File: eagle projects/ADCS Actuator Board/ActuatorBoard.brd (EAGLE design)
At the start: 91 x 91 mm, 259 parts, among them J4 OSTVN08A150, J5 OSTVN08A150, J6 OSTVN08A150, U10 TVS991, U11 BD6210F-E2, U12 ADS7841E_2K5, U13 ADS7841E_2K5, U15 TLV9051IDCKR, U16 BD6210F-E2, U17 DRV10970_MOTOR_DRIVERDRV10970, U18 DRV10970_MOTOR_DRIVERDRV10970, U19 TLV9051IDCKR, U20 DRV10970_MOTOR_DRIVERDRV10970, U21 TLV9051IDCKR, U22 BD6210F-E2, U23 TLV9051IDCKR, U24 TLV9051IDCKR, U25 ADS7841E_2K5, U26 TLV9051IDCKR, U27 ADS7841E_2K5, U28 TLV9051IDCKR, U29 TLV9051IDCKR, U30 TLV9051IDCKR, U31 TLV9051IDCKR, U32 TLV9051IDCKR, U4 ADS7841E_2K5, U6 TLV9051IDCKR, U7 TVS991, U8 TVS991, U9 ADS7841E_2K5

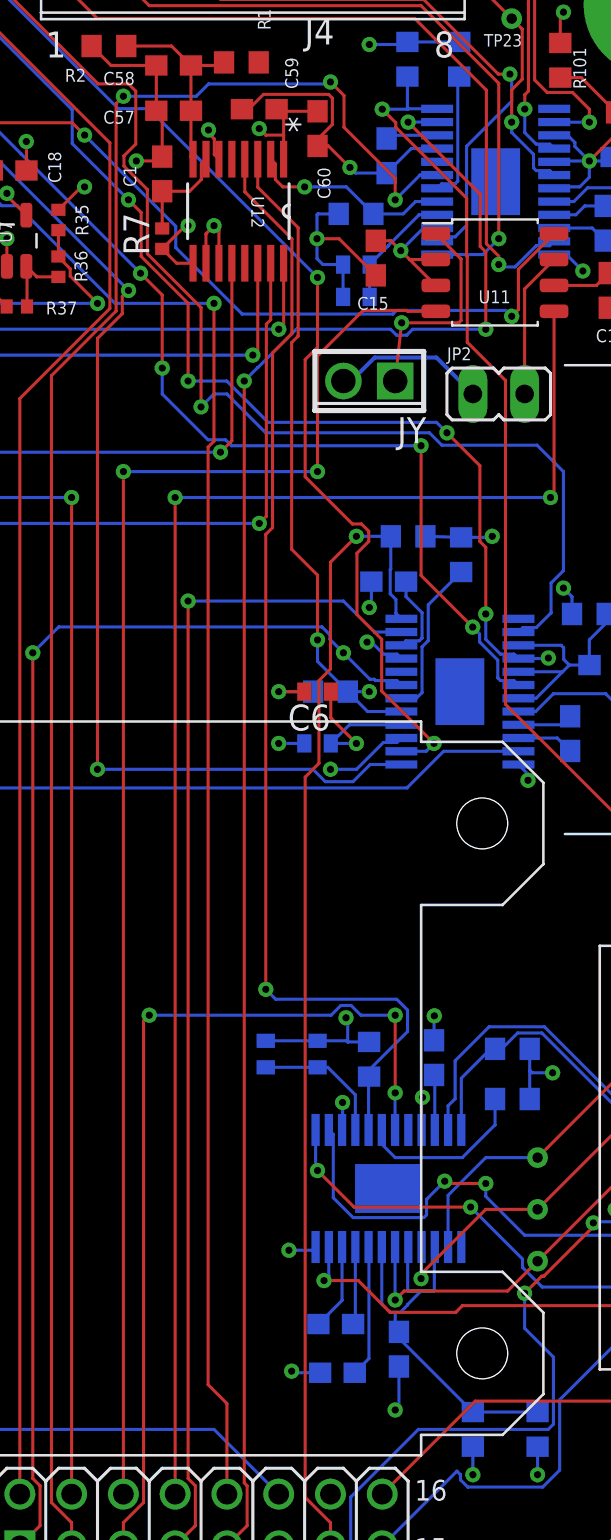
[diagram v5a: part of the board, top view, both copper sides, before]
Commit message: Fixed motordriver schematic for readability
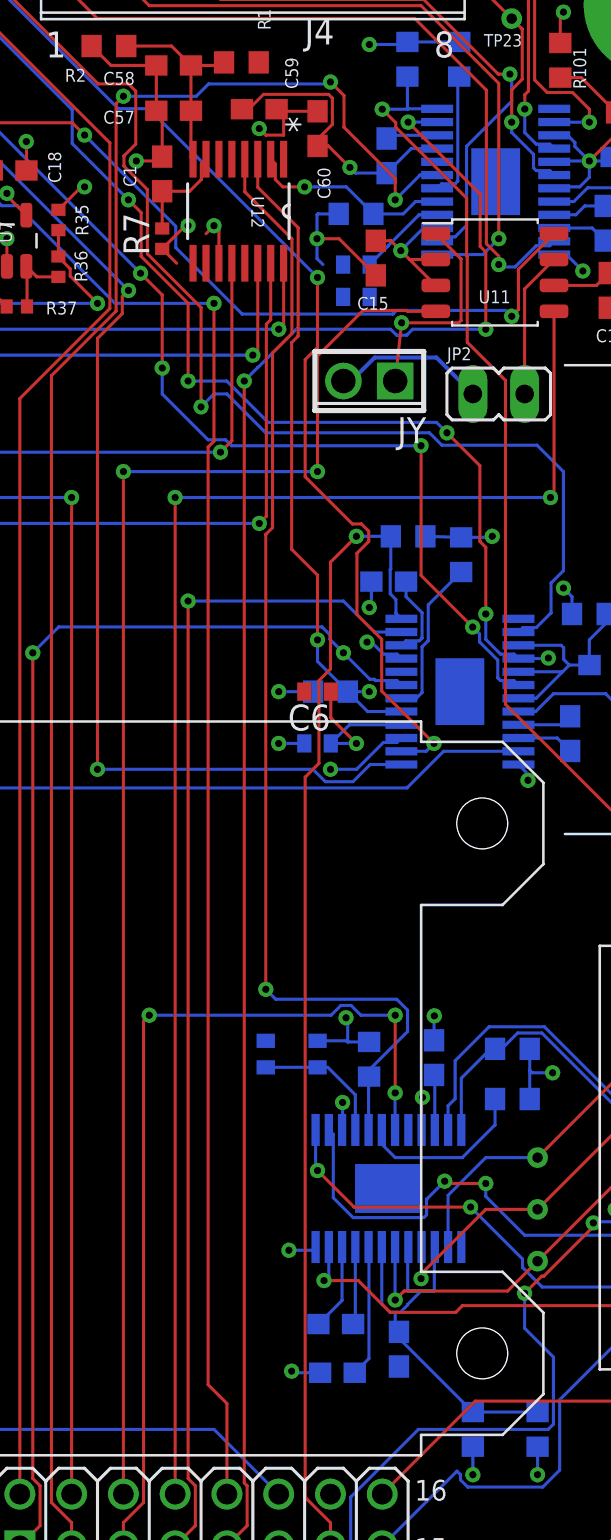
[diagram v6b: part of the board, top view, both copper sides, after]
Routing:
- net GND: track 213.5 -> 201.8 mm, vias 134 -> 132
- net +3V3: track 186.4 -> 184.4 mm
- net N$26: track 5.92 -> 4.33 mm
- net VINT/2_Z: track 20.6 -> 20.0 mm

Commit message: Formatting
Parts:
- added TP26, TP27, TP28, TP29, TP30: TESTPOINT, my_library:TP_P76H50
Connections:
- new net N$10: TP29.1, U12.5
- new net N$21: TP30.1, U9.5
- net RW_X_I_SENS: now also TP27.1
- net RW_Y_I_SENS: now also TP26.1
- net RW_Z_I_SENS: now also TP28.1

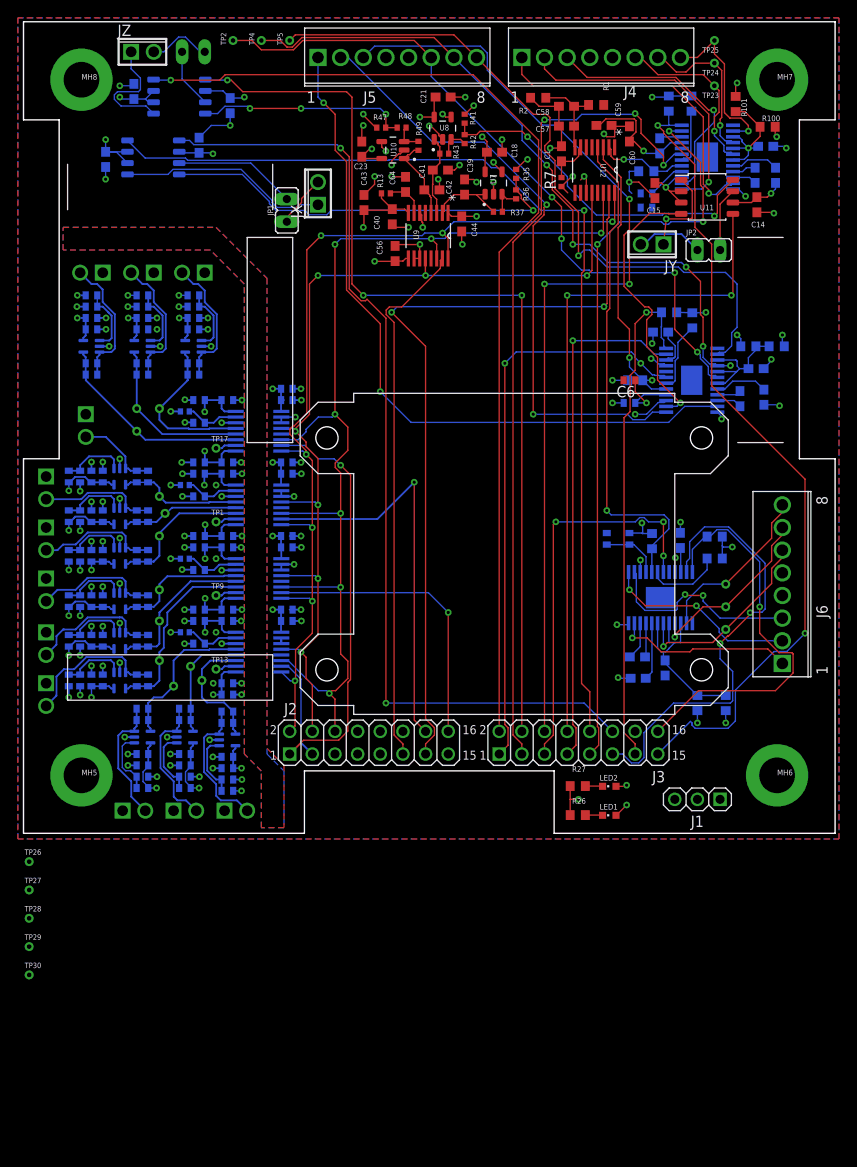
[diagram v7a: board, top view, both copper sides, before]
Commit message: Added missing decoupling caps and cleared ERC on schematic
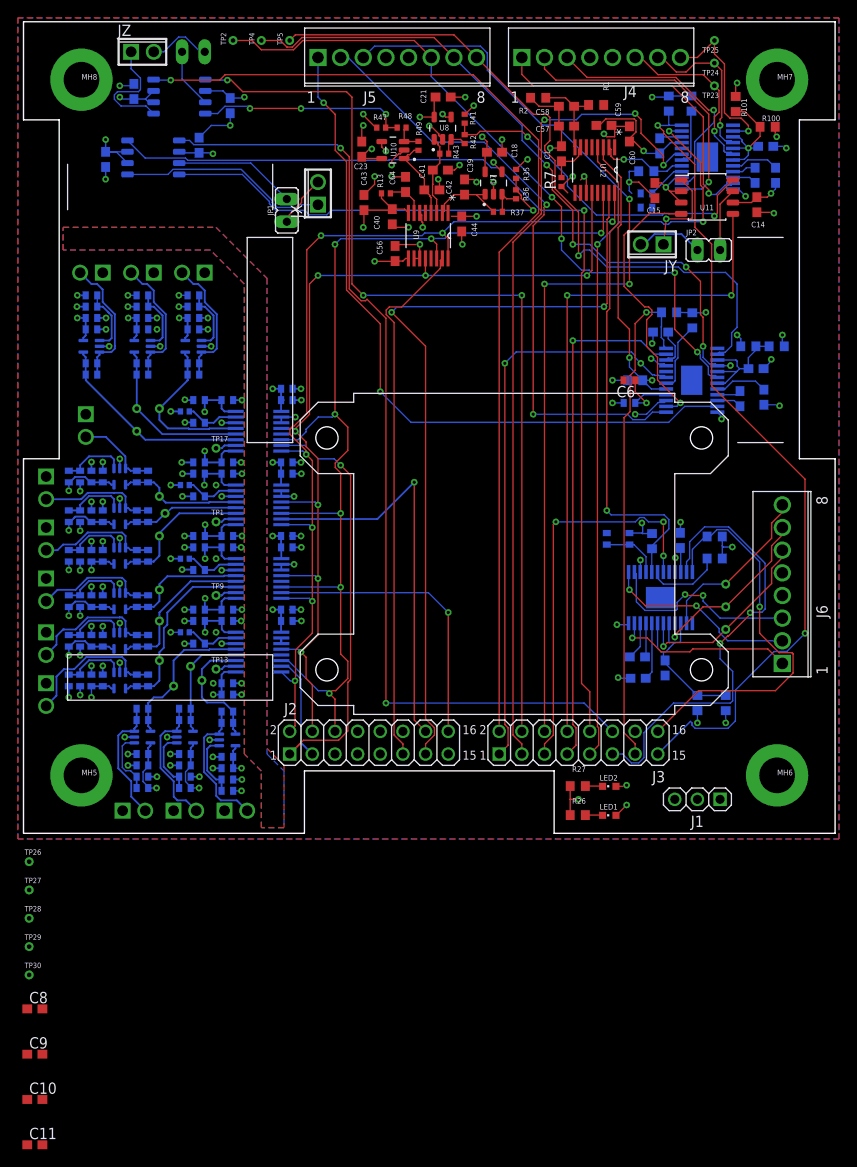
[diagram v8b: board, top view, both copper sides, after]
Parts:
- added C10, C8: 1u, rcl:C0603
- added C11, C9: 0.1u, rcl:C0603
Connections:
- removed net N$11: J2.5
- removed net N$12: J2.7
- removed net N$13: J2.9
- removed net N$16: R1.2
- removed net N$71: J2.8
- removed net N$72: J2.10
- removed net N$73: J2.12
- net +3V3: now also C10.1, C11.1, C8.1, C9.1, R1.2
- net GND: now also C10.2, C11.2, C8.2, C9.2
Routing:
- net +3V3: track 184.4 -> 183.9 mm
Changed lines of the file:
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@@
 <attribute name="NAME" x="0.127" y="-15.113" size="0.6096" layer="25" font="vector" ratio="10"/>
 </element>
+<element name="C8" library="rcl" library_urn="urn:adsk.eagle:library:334" package="C0603" package3d_urn="urn:adsk.eagle:package:23616/2" value="1u" x="1.27" y="-19.685" smashed="yes">
+<attribute name="NAME" x="0.635" y="-19.05" size="1.27" layer="25"/>
+<attribute name="POPULARITY" value="73" x="1.27" y="-19.685" size="1.778" layer="27" display="off"/>
+<attribute name="SPICEPREFIX" value="C" x="1.27" y="-19.685" size="1.778" layer="27" display="off"/>
+<attribute name="VALUE" x="0.635" y="-21.59" size="1.27" layer="27"/>
+</element>
+<element name="C9" library="rcl" library_urn="urn:adsk.eagle:library:334" package="C0603" package3d_urn="urn:adsk.eagle:package:23616/2" value="0.1u" x="1.27" y="-24.765" smashed="yes">
+<attribute name="NAME" x="0.635" y="-24.13" size="1.27" layer="25"/>
+<attribute name="POPULARITY" value="73" x="1.27" y="-24.765" size="1.778" layer="27" display="off"/>
+<attribute name="SPICEPREFIX" value="C" x="1.27" y="-24.765" size="1.778" layer="27" display="off"/>
+<attribute name="VALUE" x="0.635" y="-26.67" size="1.27" layer="27"/>
+</element>
+<element name="C10" library="rcl" library_urn="urn:adsk.eagle:library:334" package="C0603" package3d_urn="urn:adsk.eagle:package:23616/2" value="1u" x="1.27" y="-29.845" smashed="yes">
+<attribute name="NAME" x="0.635" y="-29.21" size="1.27" layer="25"/>
+<attribute name="POPULARITY" value="73" x="1.27" y="-29.845" size="1.778" layer="27" display="off"/>
+<attribute name="SPICEPREFIX" value="C" x="1.27" y="-29.845" size="1.778" layer="27" display="off"/>
+<attribute name="VALUE" x="0.635" y="-31.75" size="1.27" layer="27"/>
+</element>
+<element name="C11" library="rcl" library_urn="urn:adsk.eagle:library:334" package="C0603" package3d_urn="urn:adsk.eagle:package:23616/2" value="0.1u" x="1.27" y="-34.925" smashed="yes">
+<attribute name="NAME" x="0.635" y="-34.29" size="1.27" layer="25"/>
+<attribute name="POPULARITY" value="73" x="1.27" y="-34.925" size="1.778" layer="27" display="off"/>
+<attribute name="SPICEPREFIX" value="C" x="1.27" y="-34.925" size="1.778" layer="27" display="off"/>
+<attribute name="VALUE" x="0.635" y="-36.83" size="1.27" layer="27"/>
+</element>
 </elements>
 <signals>
@@
 <contactref element="U12" pad="10"/>
 <contactref element="C3" pad="2"/>
+<contactref element="C8" pad="2"/>
+<contactref element="C9" pad="2"/>
+<contactref element="C10" pad="2"/>
+<contactref element="C11" pad="2"/>
 <wire x1="80.9625" y1="71.4375" x2="84.0725" y2="77.0325" width="0" layer="19" extent="16-16"/>
 <wire x1="82.2325" y1="69.635" x2="80.9625" y2="71.4375" width="0" layer="19" extent="1-1"/>
@@
 <wire x1="2.54" y1="22.5425" x2="6.35" y2="20.94" width="0" layer="19" extent="16-16"/>
 <wire x1="6.985" y1="46.99" x2="7.62" y2="41.6356" width="0" layer="19" extent="1-1"/>
+<wire x1="2.12" y1="-19.685" x2="11.1125" y2="2.54" width="0" layer="19" extent="1-1"/>
+<wire x1="2.12" y1="-24.765" x2="2.12" y2="-19.685" width="0" layer="19" extent="1-1"/>
+<wire x1="2.12" y1="-29.845" x2="2.12" y2="-24.765" width="0" layer="19" extent="1-1"/>
+<wire x1="2.12" y1="-34.925" x2="2.12" y2="-29.845" width="0" layer="19" extent="1-1"/>
 </signal>
 <signal name="+5V">
@@
 <contactref element="C43" pad="1"/>
 <contactref element="C40" pad="1"/>
-<contactref element="U9" pad="1"/>
 <contactref element="U9" pad="9"/>
 <wire x1="38.175" y1="69.8775" x2="41.2375" y2="69.8775" width="0.1524" layer="1"/>
@@
 <wire x1="42.8448" y1="64.4623" x2="43.1575" y2="64.4623" width="0.1524" layer="1"/>
 <wire x1="61.0327" y1="71.8173" x2="60.325" y2="72.525" width="0.1524" layer="1"/>
-<wire x1="47.9827" y1="69.1875" x2="47.6025" y2="69.5677" width="0.1524" layer="1"/>
 <wire x1="42.7352" y1="69.99" x2="41.35" y2="69.99" width="0.1524" layer="1"/>
 <via x="16.51" y="39.0525" extent="1-16" drill="0.35"/>
@@
 <wire x1="20.3631" y1="33.3656" x2="20.3631" y2="33.655" width="0.1524" layer="16"/>
 <contactref element="U12" pad="9"/>
-<contactref element="U12" pad="1"/>
 <wire x1="61.7752" y1="71.755" x2="61.8375" y2="71.8173" width="0.1524" layer="1"/>
+<contactref element="R1" pad="2"/>
+<contactref element="C8" pad="1"/>
+<contactref element="C9" pad="1"/>
+<contactref element="U12" pad="1"/>
+<contactref element="U9" pad="1"/>
+<contactref element="C11" pad="1"/>
+<contactref element="C10" pad="1"/>
 <wire x1="67.945" y1="79.2725" x2="70.485" y2="82.55" width="0" layer="19" extent="1-1"/>
 <wire x1="66.2825" y1="76.9227" x2="65.086440625" y2="78.423559375" width="0" layer="19" extent="1-1"/>
+<wire x1="65.06" y1="81.6725" x2="65.9375" y2="79.375" width="0" layer="19" extent="1-1"/>
 <wire x1="61.595" y1="73.66" x2="66.2825" y2="76.9227" width="0" layer="19" extent="1-1"/>
 <wire x1="61.7752" y1="71.755" x2="61.0327" y2="71.8173" width="0" layer="19" extent="1-1"/>
 <wire x1="51.7575" y1="74.175" x2="60.325" y2="72.525" width="0" layer="19" extent="1-1"/>
 <wire x1="50.8" y1="69.1868" x2="51.7575" y2="74.175" width="0" layer="19" extent="1-1"/>
+<wire x1="47.6025" y1="69.5677" x2="47.9827" y2="69.1875" width="0" layer="19" extent="1-1"/>
 <wire x1="43.1575" y1="69.5677" x2="47.6025" y2="69.5677" width="0" layer="19" extent="1-1"/>
 <wire x1="40.17" y1="75.665" x2="40.14" y2="71.755" width="0" layer="19" extent="1-1"/>
@@
 <wire x1="75.565" y1="3.81" x2="67.6275" y2="5.3975" width="0" layer="19" extent="1-1"/>
 <wire x1="78.355" y1="33.275" x2="76.5175" y2="58.42" width="0" layer="19" extent="16-16"/>
+<wire x1="0.42" y1="-19.685" x2="13.985" y2="5.08" width="0" layer="19" extent="1-16"/>
+<wire x1="0.42" y1="-24.765" x2="0.42" y2="-19.685" width="0" layer="19" extent="1-1"/>
+<wire x1="0.42" y1="-29.845" x2="0.42" y2="-24.765" width="0" layer="19" extent="1-1"/>
+<wire x1="0.42" y1="-34.925" x2="0.42" y2="-29.845" width="0" layer="19" extent="1-1"/>
 </signal>
 <signal name="MAG_CUR_SEN_X">
@@
 <wire x1="60.325" y1="73.525" x2="60.325" y2="75.35" width="0.1524" layer="1"/>
 </signal>
-<signal name="N$16">
-<contactref element="R1" pad="2"/>
-</signal>
 <signal name="OUT2_Y">
 <contactref element="JP2" pad="1"/>
@@
 <wire x1="71.94" y1="19.08" x2="71.94" y2="19.39" width="0" layer="19" extent="16-16"/>
 </signal>
-<signal name="N$11">
-<contactref element="J2" pad="5"/>
-</signal>
-<signal name="N$12">
-<contactref element="J2" pad="7"/>
-</signal>
-<signal name="N$13">
-<contactref element="J2" pad="9"/>
-</signal>
-<signal name="N$71">
-<contactref element="J2" pad="8"/>
-</signal>
-<signal name="N$72">
-<contactref element="J2" pad="10"/>
-</signal>
-<signal name="N$73">
-<contactref element="J2" pad="12"/>
-</signal>
 <signal name="X+_0_DEGREES">
